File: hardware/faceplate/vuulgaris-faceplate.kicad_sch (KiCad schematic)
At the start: 12 parts, among them J1 HX JN2.54-2x5P TP H8.9, U1 MSP430FR2675TPT, Y1 32.768kHz FC-135 12.5pF

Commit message: faceplate: the 16 CapTIvate lines, their ESD network, and the pads
E1-E4 (one SCRUB_PAD_5SEG per pad), D11-D44 (TPD1E10B06DPYR) and R11-R44
(470R), and U1's sixteen CAP pins.

Allocation: each pad takes ONE PIN FROM EACH BLOCK, RXn of pad p on
CAPn.(p-1), so a pad's four elements are one measurement cycle (SLASEO5D
9.10.14; CapTIvate Technology Guide slider figure; settled f5d3b5f). The
netmap entries were generated from mklib_faceplate.py's verified pin table,
not typed: pad 1 is U1 pins 23/27/32/36, pad 2 24/28/33/37, pad 3
25/29/34/38, pad 4 26/30/35/39.

From a TI reference circuit: the network, CapTIvate Technology Guide, Design
Guide, "Electrostatic Discharge (ESD)": "Populate a 470-1k ohm resistor in
series with the electrode ... with a protection clamp such as a TVS diode
placed between the electrode and ground (return) on the electrode side of the
resistor", and TI names the TPD1E10B06. Per line: electrode net PADp_RXn,
TVS to GND, 470R, pin net CAPn.y. 470R is TI's own RX series value, the low
end of its range. 16 of each (ADR 0004): RX0's two ends are E pins 1 and 5,
both on PADp_RX0, joined ahead of the TVS.

Not from a reference circuit: E1-E4 are a placeholder symbol so the nets
exist before the copper; they have no footprint, and the copper comes from
the generator at layout. mksch.py (shared engine) now leaves an empty
footprint empty instead of writing "vuulgaris:"; the main schematic
regenerates identical apart from UUIDs (diffed), netcheck 944/944.

Checked: mksch -> netcheck 139/139, 0 unintended, 41 nets. Rendered with
kicad-cli. Board untouched.
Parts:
- added D11, D12, D13, D14, D21, D22, D23, D24, D31, D32, D33, D34, D41, D42, D43, D44: TPD1E10B06DPYR, vuulgaris:X1SON-2_DPY0002A, symbol vuulgaris:D_TVS
- added E1: scrub pad 1, symbol vuulgaris:SCRUB_PAD_5SEG
- added E2: scrub pad 2, symbol vuulgaris:SCRUB_PAD_5SEG
- added E3: scrub pad 3, symbol vuulgaris:SCRUB_PAD_5SEG
- added E4: scrub pad 4, symbol vuulgaris:SCRUB_PAD_5SEG
- added R11, R12, R13, R14, R21, R22, R23, R24, R31, R32, R33, R34, R41, R42, R43, R44: 470, vuulgaris:R0603, symbol vuulgaris:R
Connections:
- net GND: now also D11.2 (A2), D12.2 (A2), D13.2 (A2), D14.2 (A2), D21.2 (A2), D22.2 (A2), D23.2 (A2), D24.2 (A2), D31.2 (A2), D32.2 (A2), D33.2 (A2), D34.2 (A2), D41.2 (A2), D42.2 (A2), D43.2 (A2), D44.2 (A2)
- net CAP0.0: now reaches U1.23 (P3.0/TA2.2/CAP0.0)
- net CAP0.0: now also R11.2
- net CAP0.1: now reaches U1.24 (P3.3/TA2.1/CAP0.1)
- net CAP0.1: now also R21.2
- net CAP0.2: now reaches U1.25 (P2.3/TA2.0/CAP0.2)
- net CAP0.2: now also R31.2
- net CAP0.3: now reaches U1.26 (P3.4/TA2CLK/COMP0OUT/CAP0.3)
- net CAP0.3: now also R41.2
- net CAP1.0: now reaches U1.27 (P3.1/UCA1STE/CAP1.0)
- net CAP1.0: now also R12.2
- net CAP1.1: now reaches U1.28 (P2.4/UCA1CLK/CAP1.1)
- net CAP1.1: now also R22.2
- net CAP1.2: now reaches U1.29 (P2.5/UCA1RXD/UCA1SOMI/CAP1.2)
- net CAP1.2: now also R32.2
- net CAP1.3: now reaches U1.30 (P2.6/UCA1TXD/UCA1SIMO/CAP1.3)
- net CAP1.3: now also R42.2
- net CAP2.0: now reaches U1.32 (P3.7/TA3.2/CAP2.0)
- net CAP2.0: now also R13.2
- net CAP2.1: now reaches U1.33 (P4.0/TA3.1/CAP2.1)
- net CAP2.1: now also R23.2
- net CAP2.2: now reaches U1.34 (P4.1/TA3.0/CAP2.2)
- net CAP2.2: now also R33.2
- net CAP2.3: now reaches U1.35 (P4.2/TA3CLK/CAP2.3)
- net CAP2.3: now also R43.2
- net CAP3.0: now reaches U1.36 (P2.7/UCB1STE/CAP3.0)
- net CAP3.0: now also R14.2
- net CAP3.1: now reaches U1.37 (P3.5/UCB1CLK/TB0TRG/CAP3.1)
- net CAP3.1: now also R24.2
- net CAP3.2: now reaches U1.38 (P3.2/UCB1SIMO/UCB1SDA/CAP3.2)
- net CAP3.2: now also R34.2
- net CAP3.3: now reaches U1.39 (P3.6/UCB1SOMI/UCB1SCL/CAP3.3)
- net CAP3.3: now also R44.2
- new net PAD1_RX0: D11.1 (A1), E1.1 (RX0), E1.5 (RX0), R11.1
- new net PAD1_RX1: D12.1 (A1), E1.2 (RX1), R12.1
- new net PAD1_RX2: D13.1 (A1), E1.3 (RX2), R13.1
- new net PAD1_RX3: D14.1 (A1), E1.4 (RX3), R14.1
- new net PAD2_RX0: D21.1 (A1), E2.1 (RX0), E2.5 (RX0), R21.1
- new net PAD2_RX1: D22.1 (A1), E2.2 (RX1), R22.1
- new net PAD2_RX2: D23.1 (A1), E2.3 (RX2), R23.1
- new net PAD2_RX3: D24.1 (A1), E2.4 (RX3), R24.1
- new net PAD3_RX0: D31.1 (A1), E3.1 (RX0), E3.5 (RX0), R31.1
- new net PAD3_RX1: D32.1 (A1), E3.2 (RX1), R32.1
- new net PAD3_RX2: D33.1 (A1), E3.3 (RX2), R33.1
- new net PAD3_RX3: D34.1 (A1), E3.4 (RX3), R34.1
- new net PAD4_RX0: D41.1 (A1), E4.1 (RX0), E4.5 (RX0), R41.1
- new net PAD4_RX1: D42.1 (A1), E4.2 (RX1), R42.1
- new net PAD4_RX2: D43.1 (A1), E4.3 (RX2), R43.1
- new net PAD4_RX3: D44.1 (A1), E4.4 (RX3), R44.1
- no-connect marks 39 -> 23

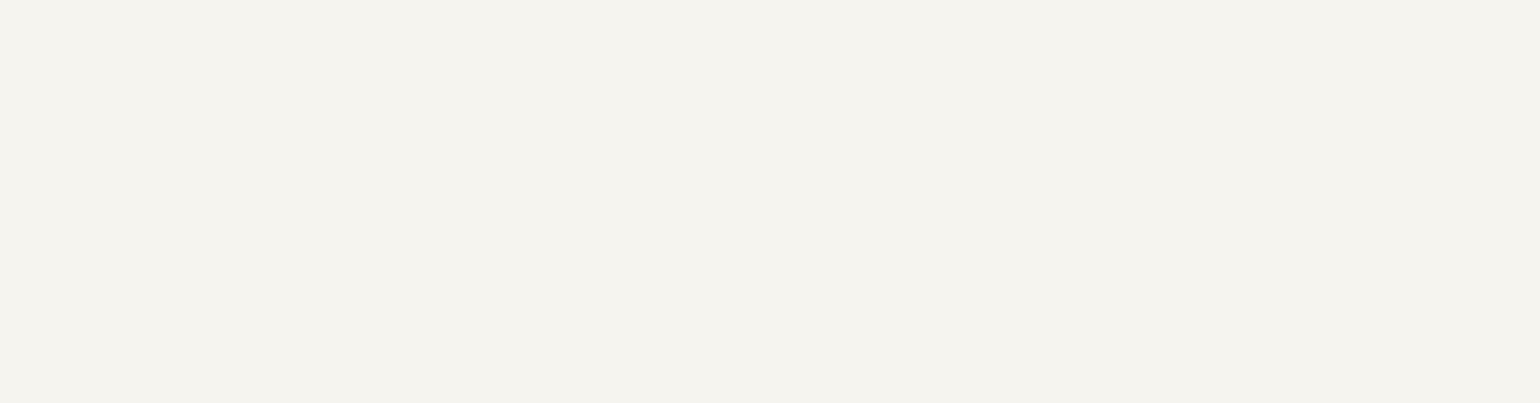
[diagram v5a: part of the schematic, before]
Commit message: faceplate: SBW pads and UART test points
TP1-TP6, bare 1.5mm SMD pads (the main board's TestPoint_Pad_D1.5mm, never
populated, off the BOM and the placement file): TP1 MSP_TEST, TP2 MSP_RST,
TP3 P3V3_MSP430, TP4 GND -- the Spy-Bi-Wire recovery set, the four signals of
SLASEO5D Figure 10-4 -- and TP5 MSP430_TXD, TP6 MSP430_RXD. The SBW TEST and
RST pads are also the RST and TEST test points; a second pad on each net adds
nothing, so six pads rather than eight. SMD because a through-hole pad would
show on the front.

Not from a reference circuit: TI names the SBW signals but no pad pattern.
Their spacing is layout's (a 2.54mm row takes a pogo strip or a header).

The schematic phase is complete. U1 wires 25 pins; 6-22 and 40-45 are unused
GPIO, which SLASEO5D Table 7-4 terminates in firmware, not on the board.

Checked: mksch -> netcheck 145/145, 0 unintended, 41 nets. boardcheck: 0
unconnected, 0 clearance, 0 pads on unasked nets; its 135 parity mismatches
are exactly the netmap pins of parts not yet on the board (everything but
J1), as expected until layout. DRC 0/0, panelcheck 6 OK. Board untouched.
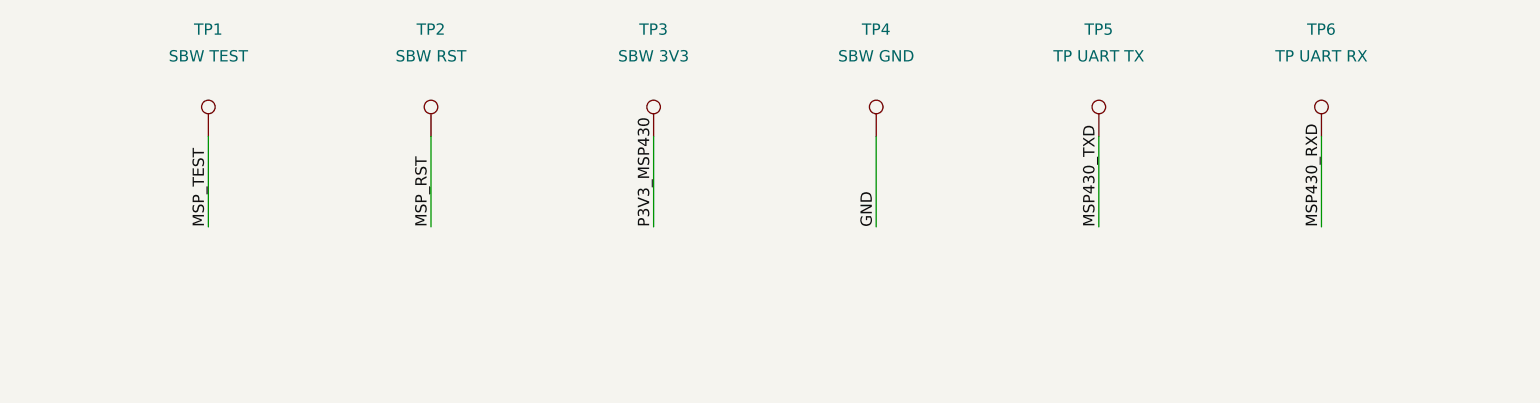
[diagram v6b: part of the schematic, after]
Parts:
- added TP1: SBW TEST, vuulgaris:TestPoint_Pad_D1.5mm, symbol vuulgaris:TestPoint
- added TP2: SBW RST, vuulgaris:TestPoint_Pad_D1.5mm, symbol vuulgaris:TestPoint
- added TP3: SBW 3V3, vuulgaris:TestPoint_Pad_D1.5mm, symbol vuulgaris:TestPoint
- added TP4: SBW GND, vuulgaris:TestPoint_Pad_D1.5mm, symbol vuulgaris:TestPoint
- added TP5: TP UART TX, vuulgaris:TestPoint_Pad_D1.5mm, symbol vuulgaris:TestPoint
- added TP6: TP UART RX, vuulgaris:TestPoint_Pad_D1.5mm, symbol vuulgaris:TestPoint
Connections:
- net GND: now also TP4.1
- net MSP430_RXD: now also TP6.1
- net MSP430_TXD: now also TP5.1
- net MSP_RST: now also TP2.1
- net MSP_TEST: now also TP1.1
- net P3V3_MSP430: now also TP3.1
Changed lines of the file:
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@@
     (pin "2")
+  )
+  (symbol (lib_id "vuulgaris:TestPoint") (at 180 100 0) (unit 1)
+    (in_bom yes) (on_board yes) (dnp no)
+    (property "Reference" "TP1" (at 180 88 0) (effects (font (size 1.27 1.27))))
+    (property "Value" "SBW TEST" (at 180 91 0) (effects (font (size 1.27 1.27))))
+    (property "Footprint" "vuulgaris:TestPoint_Pad_D1.5mm" (at 180 100 0) (effects (font (size 1.27 1.27)) hide))
+    (property "Datasheet" "" (at 180 100 0) (effects (font (size 1.27 1.27)) hide))
+    (pin "1")
+  )
+  (symbol (lib_id "vuulgaris:TestPoint") (at 205 100 0) (unit 1)
+    (in_bom yes) (on_board yes) (dnp no)
+    (property "Reference" "TP2" (at 205 88 0) (effects (font (size 1.27 1.27))))
+    (property "Value" "SBW RST" (at 205 91 0) (effects (font (size 1.27 1.27))))
+    (property "Footprint" "vuulgaris:TestPoint_Pad_D1.5mm" (at 205 100 0) (effects (font (size 1.27 1.27)) hide))
+    (property "Datasheet" "" (at 205 100 0) (effects (font (size 1.27 1.27)) hide))
+    (pin "1")
+  )
+  (symbol (lib_id "vuulgaris:TestPoint") (at 230 100 0) (unit 1)
+    (in_bom yes) (on_board yes) (dnp no)
+    (property "Reference" "TP3" (at 230 88 0) (effects (font (size 1.27 1.27))))
+    (property "Value" "SBW 3V3" (at 230 91 0) (effects (font (size 1.27 1.27))))
+    (property "Footprint" "vuulgaris:TestPoint_Pad_D1.5mm" (at 230 100 0) (effects (font (size 1.27 1.27)) hide))
+    (property "Datasheet" "" (at 230 100 0) (effects (font (size 1.27 1.27)) hide))
+    (pin "1")
+  )
+  (symbol (lib_id "vuulgaris:TestPoint") (at 255 100 0) (unit 1)
+    (in_bom yes) (on_board yes) (dnp no)
+    (property "Reference" "TP4" (at 255 88 0) (effects (font (size 1.27 1.27))))
+    (property "Value" "SBW GND" (at 255 91 0) (effects (font (size 1.27 1.27))))
+    (property "Footprint" "vuulgaris:TestPoint_Pad_D1.5mm" (at 255 100 0) (effects (font (size 1.27 1.27)) hide))
+    (property "Datasheet" "" (at 255 100 0) (effects (font (size 1.27 1.27)) hide))
+    (pin "1")
+  )
+  (symbol (lib_id "vuulgaris:TestPoint") (at 280 100 0) (unit 1)
+    (in_bom yes) (on_board yes) (dnp no)
+    (property "Reference" "TP5" (at 280 88 0) (effects (font (size 1.27 1.27))))
+    (property "Value" "TP UART TX" (at 280 91 0) (effects (font (size 1.27 1.27))))
+    (property "Footprint" "vuulgaris:TestPoint_Pad_D1.5mm" (at 280 100 0) (effects (font (size 1.27 1.27)) hide))
+    (property "Datasheet" "" (at 280 100 0) (effects (font (size 1.27 1.27)) hide))
+    (pin "1")
+  )
+  (symbol (lib_id "vuulgaris:TestPoint") (at 305 100 0) (unit 1)
+    (in_bom yes) (on_board yes) (dnp no)
+    (property "Reference" "TP6" (at 305 88 0) (effects (font (size 1.27 1.27))))
+    (property "Value" "TP UART RX" (at 305 91 0) (effects (font (size 1.27 1.27))))
+    (property "Footprint" "vuulgaris:TestPoint_Pad_D1.5mm" (at 305 100 0) (effects (font (size 1.27 1.27)) hide))
+    (property "Datasheet" "" (at 305 100 0) (effects (font (size 1.27 1.27)) hide))
+    (pin "1")
   )
   (symbol (lib_id "vuulgaris:MSP430FR2675TPT") (at 330 220 0) (unit 1)
@@
   (wire (pts (xy 495.0 551.19) (xy 495.0 541.03)) (stroke (width 0) (type solid)))
   (wire (pts (xy 495.0 558.81) (xy 495.0 568.97)) (stroke (width 0) (type solid)))
+  (wire (pts (xy 180.0 100.0) (xy 180.0 110.16)) (stroke (width 0) (type solid)))
+  (wire (pts (xy 205.0 100.0) (xy 205.0 110.16)) (stroke (width 0) (type solid)))
+  (wire (pts (xy 230.0 100.0) (xy 230.0 110.16)) (stroke (width 0) (type solid)))
+  (wire (pts (xy 255.0 100.0) (xy 255.0 110.16)) (stroke (width 0) (type solid)))
+  (wire (pts (xy 280.0 100.0) (xy 280.0 110.16)) (stroke (width 0) (type solid)))
+  (wire (pts (xy 305.0 100.0) (xy 305.0 110.16)) (stroke (width 0) (type solid)))
   (wire (pts (xy 279.2 184.44) (xy 269.04 184.44)) (stroke (width 0) (type solid)))
   (wire (pts (xy 279.2 186.98) (xy 269.04 186.98)) (stroke (width 0) (type solid)))
@@
     (effects (font (size 1.27 1.27)) (justify left bottom))
   )
+  (label "MSP_TEST" (at 180.0 110.16 270) (fields_autoplaced)
+    (effects (font (size 1.27 1.27)) (justify left bottom))
+  )
+  (label "MSP_RST" (at 205.0 110.16 270) (fields_autoplaced)
+    (effects (font (size 1.27 1.27)) (justify left bottom))
+  )
+  (label "P3V3_MSP430" (at 230.0 110.16 270) (fields_autoplaced)
+    (effects (font (size 1.27 1.27)) (justify left bottom))
+  )
+  (label "GND" (at 255.0 110.16 270) (fields_autoplaced)
+    (effects (font (size 1.27 1.27)) (justify left bottom))
+  )
+  (label "MSP430_TXD" (at 280.0 110.16 270) (fields_autoplaced)
+    (effects (font (size 1.27 1.27)) (justify left bottom))
+  )
+  (label "MSP430_RXD" (at 305.0 110.16 270) (fields_autoplaced)
+    (effects (font (size 1.27 1.27)) (justify left bottom))
+  )

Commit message: faceplate: C4, the RST capacitor, is a 1nF C0G 5% (C163508)
SLASEO5D Figure 10-4 wants 1nF on RST/NMI/SBWTDIO with "The upper limit for
C1 is 1.1 nF when using current TI tools", so tolerance decides the part.
The only Basic 1nF 0603 at JLC (checked in its library 2026-09-28) is C1588,
X7R +-10%: 1.1nF worst case before any pin or trace capacitance, and X7R's
+-15% over temperature on top. C163508, Samsung CL10C102JB8NNNC, C0G +-5%,
567k in stock, tops out at 1.05nF and does not drift. It is Extended, and it
is the part the main board already carries as "1nF C0G", so the value string
matches mkbom.py's CURATED key.

Checked: mksch -> netcheck 145/145, 0 unintended.
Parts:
- C4: value 1nF -> 1nF C0G
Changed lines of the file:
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@@
     (in_bom yes) (on_board yes) (dnp no)
     (property "Reference" "C4" (at 265 288 0) (effects (font (size 1.27 1.27))))
-    (property "Value" "1nF" (at 265 291 0) (effects (font (size 1.27 1.27))))
+    (property "Value" "1nF C0G" (at 265 291 0) (effects (font (size 1.27 1.27))))
     (property "Footprint" "vuulgaris:C0603" (at 265 300 0) (effects (font (size 1.27 1.27)) hide))
     (property "Datasheet" "" (at 265 300 0) (effects (font (size 1.27 1.27)) hide))
